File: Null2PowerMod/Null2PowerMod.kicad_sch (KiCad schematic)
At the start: 33 parts, among them J1 Conn_01x01, J2 USB_C_Receptacle_USB2.0, J3 Conn_01x01, J5 JST 2-PH, J6 Conn_01x01, U1 MCP73871, U2 TPS61030PWP, U3 MMUN2133LT1G

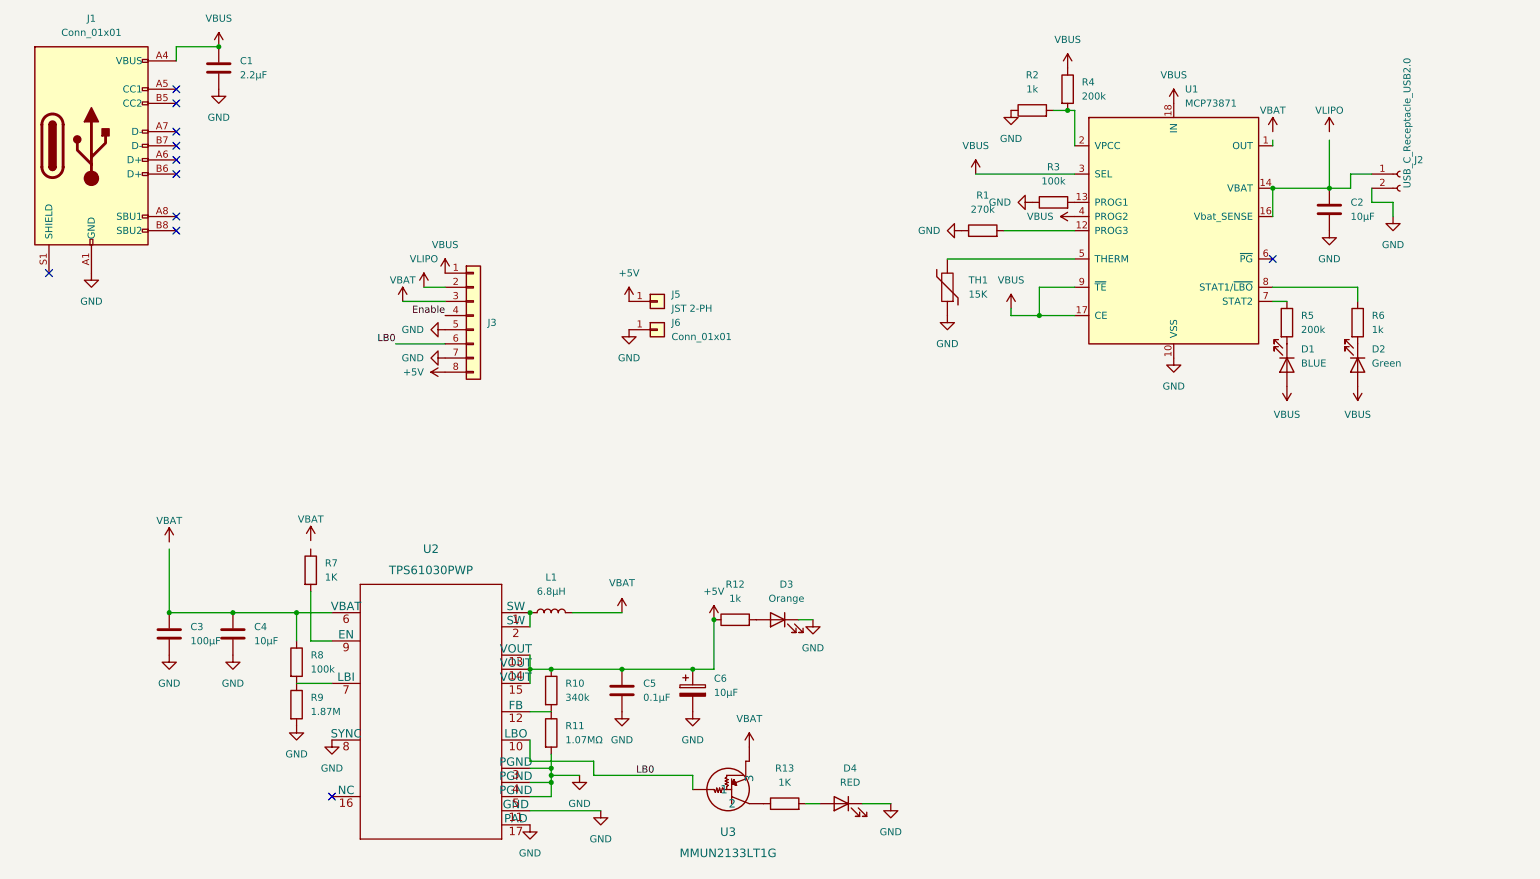
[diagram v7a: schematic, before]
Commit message: updating schematic, re-starting the pcb completly
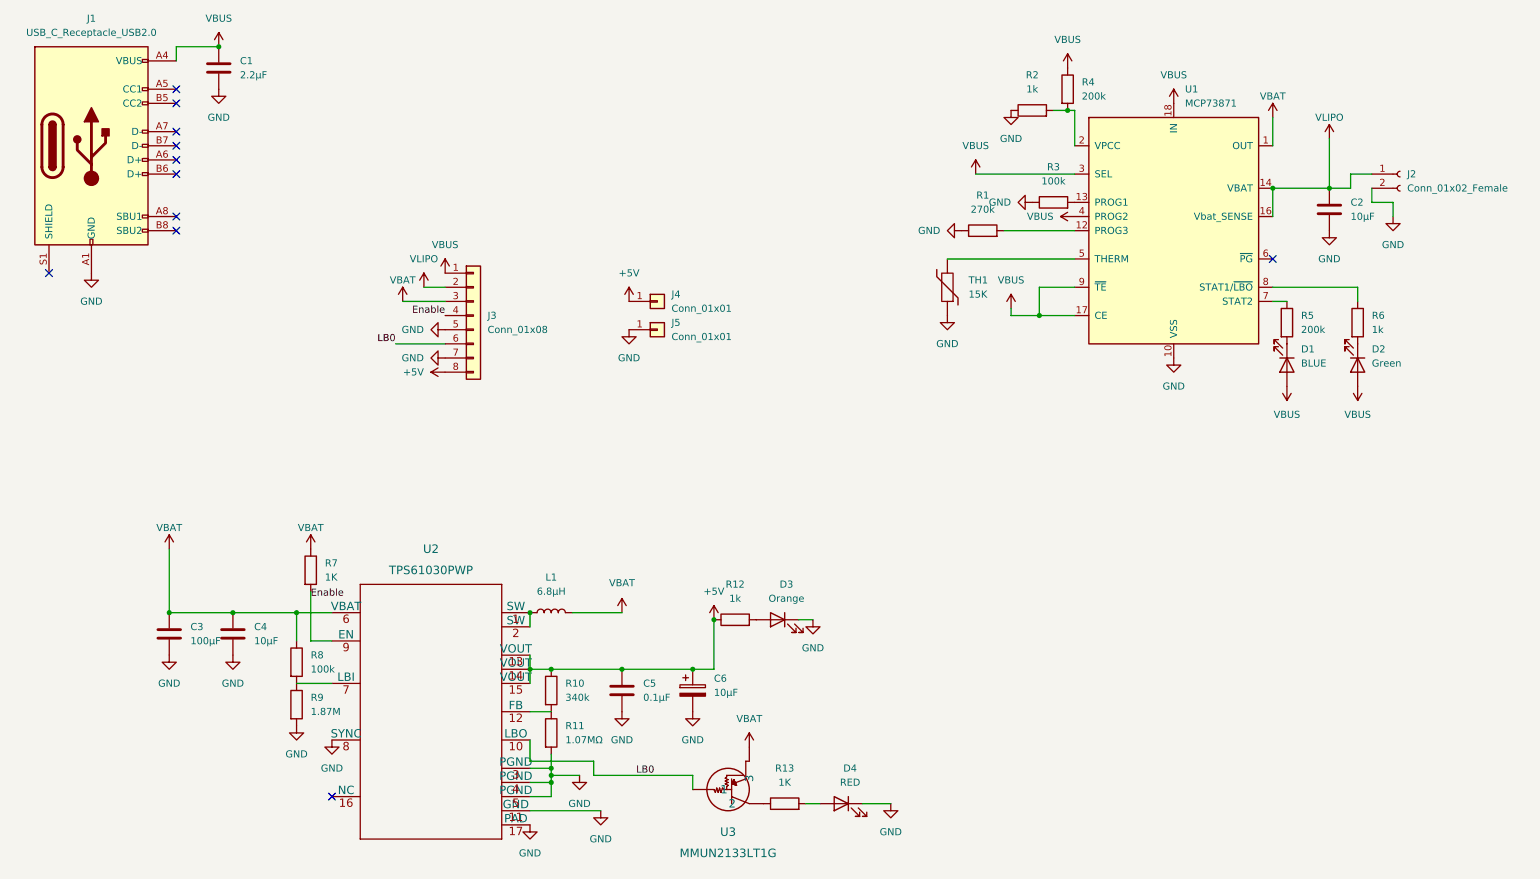
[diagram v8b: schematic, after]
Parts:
- removed J6: Conn_01x01, Connector_PinHeader_2.54mm:PinHeader_1x01_P2.54mm_Vertical, symbol Connector_Generic:Conn_01x01
- added J4: Conn_01x01, Connector_PinHeader_2.54mm:PinHeader_1x01_P2.54mm_Vertical, symbol Connector_Generic:Conn_01x01
- J1: value Conn_01x01 -> USB_C_Receptacle_USB2.0; footprint Connector_PinHeader_2.54mm:PinHeader_1x01_P2.54mm_Vertical -> Connector_USB:USB_C_Receptacle_GCT_USB4085
- J2: value USB_C_Receptacle_USB2.0 -> Conn_01x02_Female; footprint Connector_USB:USB_C_Receptacle_GCT_USB4085 -> Connector_JST:JST_EH_S2B-EH_1x02_P2.50mm_Horizontal
- J3: value Conn_01x01 -> Conn_01x08; footprint Connector_PinHeader_2.54mm:PinHeader_1x01_P2.54mm_Vertical -> Connector_PinHeader_1.00mm:PinHeader_1x08_P1.00mm_Vertical
- J5: value JST 2-PH -> Conn_01x01; footprint Connector_JST:JST_EH_S2B-EH_1x02_P2.50mm_Horizontal -> Connector_PinHeader_2.54mm:PinHeader_1x01_P2.54mm_Vertical
- L1: footprint Inductor_SMD:L_0201_0603Metric -> VLC5045:VLC5045T-4R7M
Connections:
- net +5V: now also J4.1 (Pin_1); no longer J5.1 (Pin_1)
- net Enable: now also R7.2, U2.9 (EN)
- net GND: now also J5.1 (Pin_1)
- net VBAT: now also C3.1, C4.1, R7.1, R8.1, U1.1 (OUT), U1.20 (OUT), U2.6 (VBAT)
- net VLIPO: now also C2.1, J2.1 (Pin_1), U1.14 (VBAT), U1.15 (VBAT), U1.16 (Vbat_SENSE)
